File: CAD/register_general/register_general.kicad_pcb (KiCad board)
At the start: 4 copper layers, 76 x 28 mm, 29 parts, among them J1 Conn_01x16_Pin, J2 Conn_01x16_Pin, J3 load select, J4 output select, U1 74HC245, U2 74HC377

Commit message: add NetClasses, TestPads, remove jumper pins
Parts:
- removed J3: load select, Connector_PinHeader_2.54mm:PinHeader_1x03_P2.54mm_Vertical
- removed J4: output select, Connector_PinHeader_2.54mm:PinHeader_1x03_P2.54mm_Vertical
- added TP1: 5V, TestPoint:TestPoint_THTPad_D1.0mm_Drill0.5mm, F.Cu at (95.7, 68.2)
- added TP2: GND, TestPoint:TestPoint_THTPad_D1.0mm_Drill0.5mm, F.Cu at (91.7, 85.4)
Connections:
- J2 pad 1: reg2_out -> unconnected-(J2-Pin_1-Pad1)
- J2 pad 2: reg2_in -> unconnected-(J2-Pin_2-Pad2)
- J2 pad 3: reg1_out -> reg2_out
- J2 pad 4: reg1_in -> reg2_in
- R10 pad 1: Net-(J4-Pin_2) -> reg1_out
- R9 pad 1: Net-(J3-Pin_2) -> reg1_in
- U1 pad 19: Net-(J4-Pin_2) -> reg1_out
- U2 pad 1: Net-(J3-Pin_2) -> reg1_in
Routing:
- net Net-(J4-Pin_2): track 62.9 -> 0.00 mm, vias 3 -> 0
- net Net-(J3-Pin_2): track 46.0 -> 0.00 mm, vias 2 -> 0
- net reg1_in: track 71.0 -> 54.5 mm, vias 1 -> 2
- net reg1_out: track 65.1 -> 67.9 mm, vias 1 -> 2
- net +5V: track 148.9 -> 151.2 mm
- net reg2_in: track 69.5 -> 70.2 mm
- net GND: vias 106 -> 102
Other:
- copper layers 4 -> 2
- board text added: "5V"
- board text added: "GND"
- board text removed: "I"
- board text removed: "II"
- board text removed: "in"
- board text removed: "out"

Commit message: fix HC245 dir signal
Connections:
- U1 pad 1: GND -> +5V
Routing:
- net +5V: track 151.2 -> 154.8 mm
- net GND: vias 102 -> 104

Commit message: add text variables for revision, etc.
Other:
- board text added: "Rev ${REVISION} ${YEAR}/${MONTH}"
- board text removed: "Rev 1.0 2026/03"
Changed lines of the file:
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@@
 		)
 	)
+	(property "DAY" "03")
+	(property "MONTH" "03")
+	(property "REVISION" "1.0")
+	(property "YEAR" "2026")
 	(net 0 "")
 	(net 1 "GND")
@@
 		)
 	)
-	(gr_text "Rev 1.0\n2026/03"
+	(gr_text "Rev ${REVISION}\n${YEAR}/${MONTH}"
 		(at 152.65 80.335001 90)
 		(layer "B.SilkS" knockout)

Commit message: update silkscreen qr code, license, add images
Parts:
- added G***: Github QR Code, LOGO, B.Cu at (112.4, 86.6)
- added Ref**: Val**, 8-bit_computer:by-nc-sa.eu, B.Cu at (112.5, 69.6)
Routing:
- net GND: vias 104 -> 103

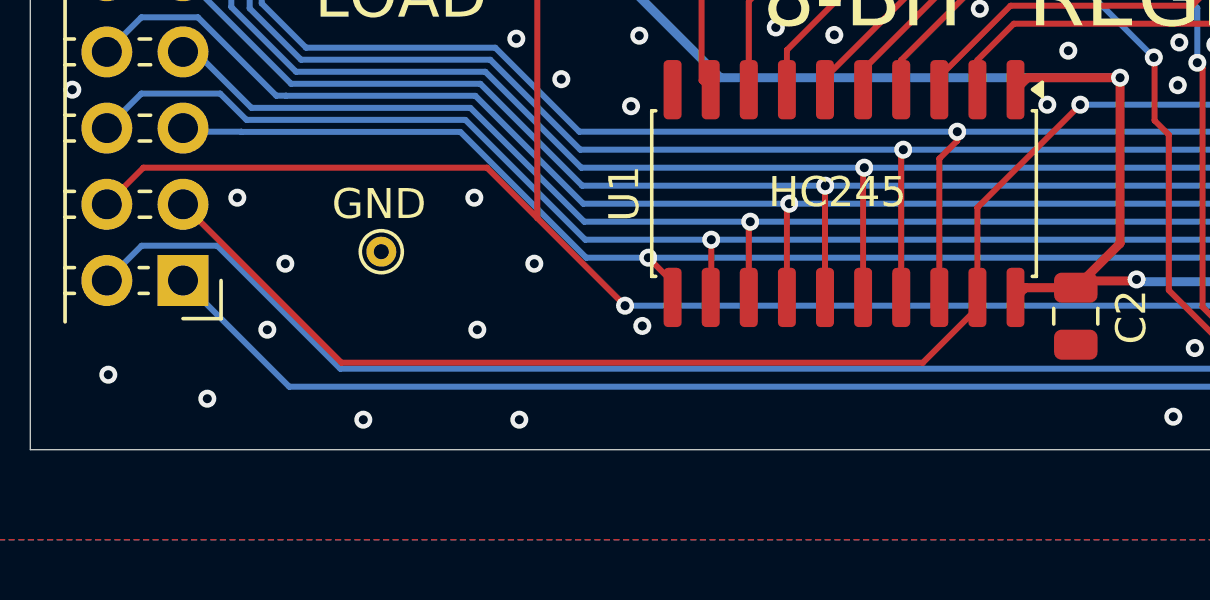
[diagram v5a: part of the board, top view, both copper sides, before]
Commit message: add pull-up resistor to general register
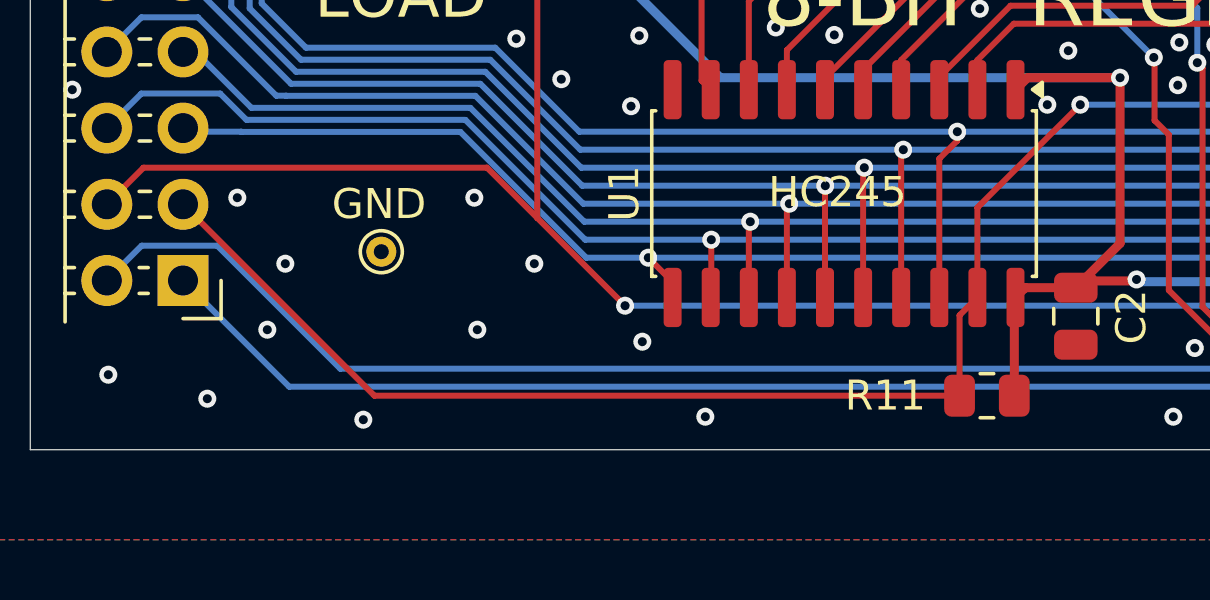
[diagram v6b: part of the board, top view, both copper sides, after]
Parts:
- added R11: 10k, Resistor_SMD:R_0805_2012Metric, F.Cu at (111.9, 90.2)
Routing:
- net +5V: track 154.8 -> 158.1 mm
- net reg1_out: track 67.9 -> 70.5 mm

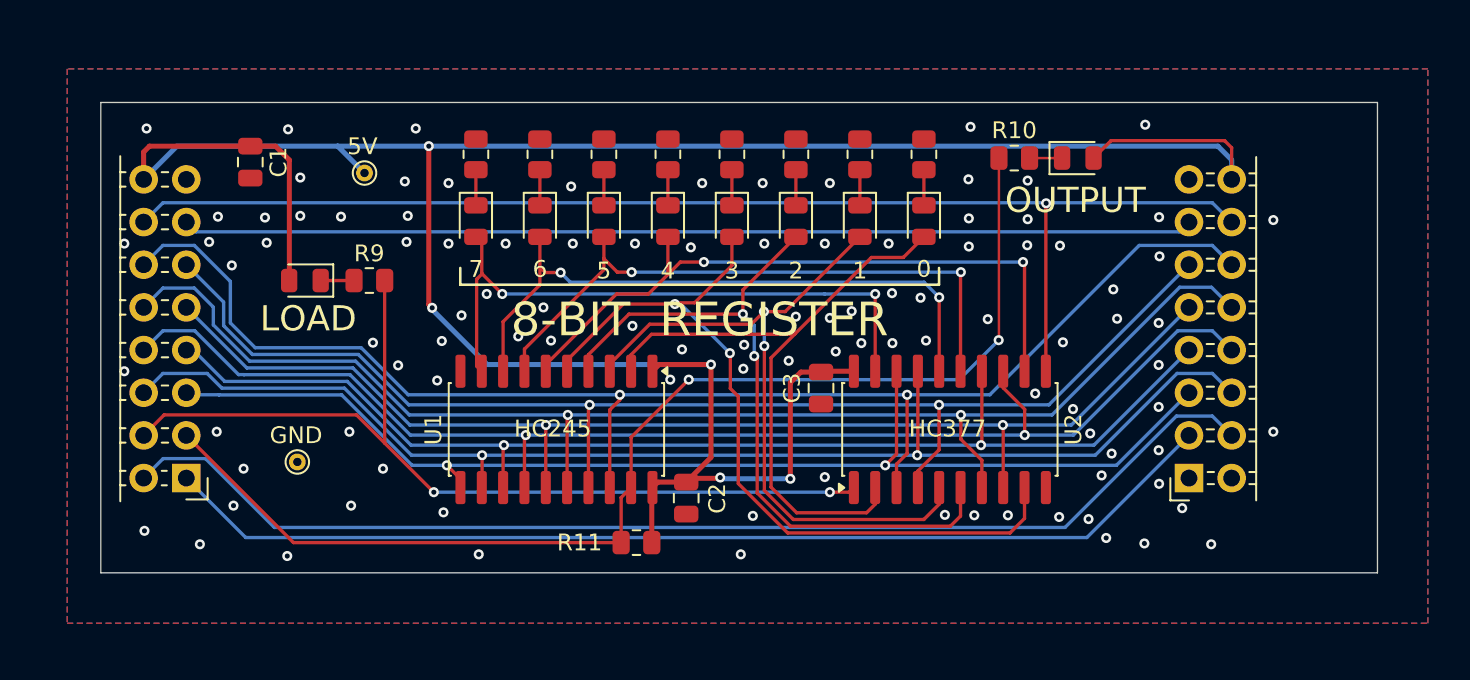
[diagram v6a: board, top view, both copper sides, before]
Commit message: update General Register, add mounting holes, testpoints, LCSC numbers
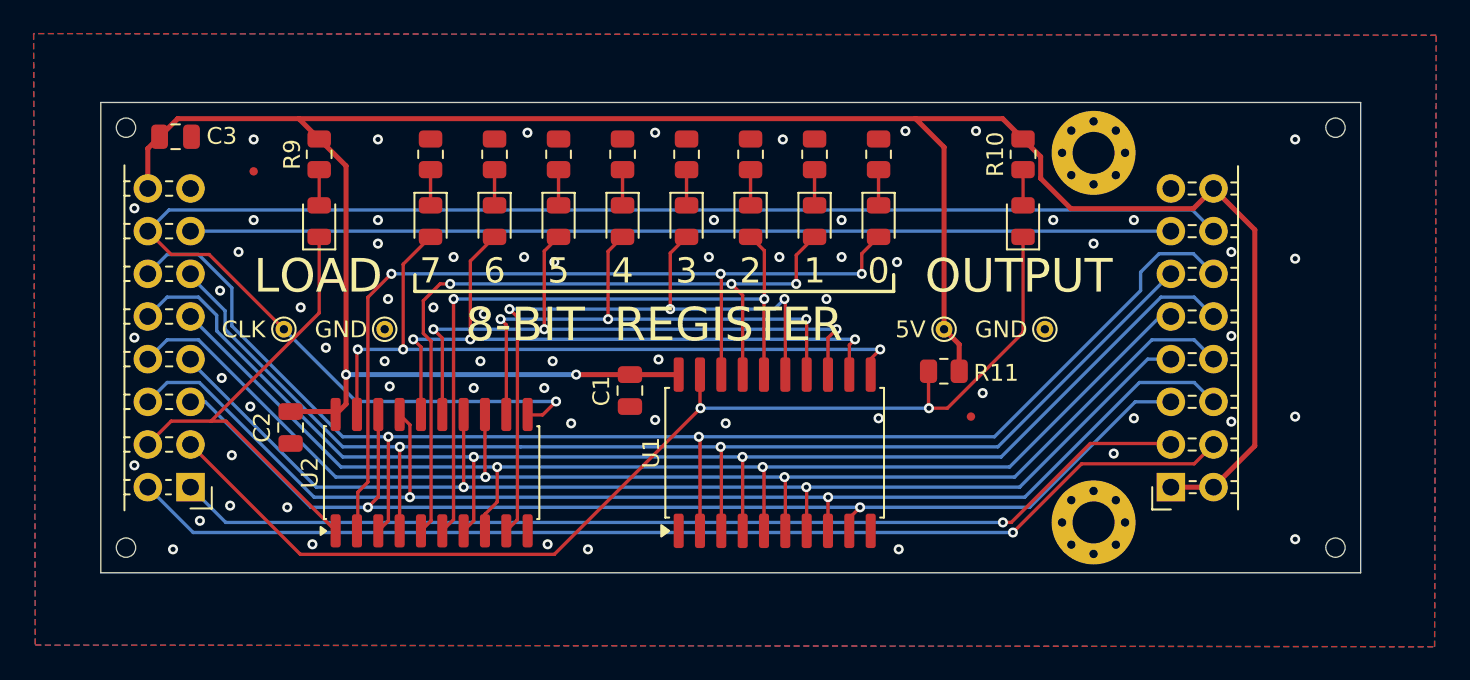
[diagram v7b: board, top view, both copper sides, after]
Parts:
- removed the G*** at (112.4, 86.6)
- added FID1: Fiducial, Fiducial:Fiducial_0.5mm_Mask1mm, F.Cu at (89.1, 68.1)
- added FID2: Fiducial, Fiducial:Fiducial_0.5mm_Mask1mm, F.Cu at (131.8, 82.7)
- added G***: LOGO, 8-bit_computer:qr-code-github, B.Cu at (111.4, 70.3)
- added H1: MountingHole_Pad, MountingHole:MountingHole_2.5mm_Pad_Via, F.Cu at (139.1, 89.0)
- added H2: MountingHole_Pad, MountingHole:MountingHole_2.5mm_Pad_Via, F.Cu at (139.1, 67.0)
- added H3: ToolingHole, MountingHole:ToolingHole_1.152mm, F.Cu at (81.5, 65.5)
- added H4: ToolingHole, MountingHole:ToolingHole_1.152mm, F.Cu at (81.5, 90.5)
- added H5: ToolingHole, MountingHole:ToolingHole_1.152mm, F.Cu at (153.5, 65.5)
- added H6: ToolingHole, MountingHole:ToolingHole_1.152mm, F.Cu at (153.5, 90.5)
- added TP3: TestPoint, TestPoint:TestPoint_THTPad_D1.0mm_Drill0.5mm, F.Cu at (90.9, 77.5)
- added TP4: TestPoint, TestPoint:TestPoint_THTPad_D1.0mm_Drill0.5mm, F.Cu at (96.9, 77.5)
- D10: value LED -> OUT
- D9: value LED -> IN
- TP1: value 5V -> TestPoint
- TP2: value GND -> TestPoint
- U1: footprint Package_SO:SO-20_5.3x12.6mm_P1.27mm -> Package_SO:SOIC-20W_7.5x12.8mm_P1.27mm
- U2: footprint Package_SO:SO-20_5.3x12.6mm_P1.27mm -> 8-bit_computer:SO-20_5.3x12.6mm_P1.27mm
- moved TP2 45.2 mm to (136.2, 77.5)
- moved TP1 35.7 mm to (130.2, 77.5)
- moved C2 31.7 mm to (91.3, 83.3)
- moved U2 31.0 mm to (99.7, 86.0)
- moved Ref** 23.0 mm to (132.0, 81.8)
- moved R11 21.0 mm to (130.2, 80.0)
- moved U1 13.1 mm to (120.1, 84.8), turned to 90 degrees
- moved R9 8.08 mm to (93.0, 67.1), turned to -90 degrees
- moved C1 7.22 mm to (111.5, 81.2)
- moved D10 4.97 mm to (134.9, 71.1), turned to 90 degrees
- moved C3 4.70 mm to (84.5, 66.0), turned to 0 degrees
- moved D9 3.64 mm to (93.0, 71.1), turned to 90 degrees
- moved D1 2.70 mm to (126.3, 71.1)
- moved D2 2.70 mm to (122.5, 71.1)
- moved D5 2.70 mm to (111.1, 71.1)
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- renumbered C2 to C1, C3 to C2, C1 to C3
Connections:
- net reg2_in renamed ~{reg2_in}
- net reg2_out renamed ~{reg2_out}
- net rst renamed ~{rst}
- D10 pad 1: Net-(D10-K) -> ~{reg1_out}
- D10 pad 2: +5V -> Net-(D10-A)
- D9 pad 1: Net-(D9-K) -> ~{reg1_in}
- D9 pad 2: +5V -> Net-(D9-A)
- J1 pad 3: reg1_out -> ~{reg1_out}
- J1 pad 4: reg1_in -> ~{reg1_in}
- J2 pad 1: unconnected-(J2-Pin_1-Pad1) -> +5V
- J2 pad 2: unconnected-(J2-Pin_2-Pad2) -> +5V
- R10 pad 1: reg1_out -> Net-(D10-A)
- R10 pad 2: Net-(D10-K) -> +5V
- R11 pad 1: reg1_out -> ~{reg1_out}
- R9 pad 1: reg1_in -> +5V
- R9 pad 2: Net-(D9-K) -> Net-(D9-A)
- U1 pad 1: +5V -> GND
- U1 pad 11: /dbus7 -> /q7
- U1 pad 12: /dbus6 -> /q6
- U1 pad 13: /dbus5 -> /q5
- U1 pad 14: /dbus4 -> /q4
- U1 pad 15: /dbus3 -> /q3
- U1 pad 16: /dbus2 -> /q2
- U1 pad 17: /dbus1 -> /q1
- U1 pad 18: /dbus0 -> /q0
- U1 pad 19: reg1_out -> ~{reg1_out}
- U1 pad 2: /q0 -> /dbus0
- U1 pad 3: /q1 -> /dbus1
- U1 pad 4: /q2 -> /dbus2
- U1 pad 5: /q3 -> /dbus3
- U1 pad 6: /q4 -> /dbus4
- U1 pad 7: /q5 -> /dbus5
- U1 pad 8: /q6 -> /dbus6
- U1 pad 9: /q7 -> /dbus7
- U2 pad 1: reg1_in -> ~{reg1_in}
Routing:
- net reg1_out: track 70.5 -> 0.00 mm, vias 2 -> 0
- net ~{reg1_out}: track 0.00 -> 67.7 mm, vias 0 -> 2
- net reg1_in: track 54.5 -> 0.00 mm, vias 2 -> 0
- net ~{reg1_in}: track 0.00 -> 28.1 mm
- net clk: track 75.8 -> 95.0 mm
- net /q0: track 39.0 -> 52.8 mm, vias 0 -> 3
- net +5V: track 158.1 -> 150.1 mm, vias 5 -> 2
- net /q7: track 36.4 -> 44.1 mm, vias 2 -> 3
- net /q3: track 46.8 -> 39.5 mm, vias 2 -> 3
- net /q4: track 39.7 -> 32.6 mm, vias 2 -> 3
- net /q1: track 41.2 -> 45.7 mm, vias 2 -> 3
- net ~{reg2_in}: track 70.2 -> 66.7 mm, vias 0 -> 1
- net ~{reg2_out}: track 63.7 -> 61.2 mm, vias 0 -> 1
- net Net-(D9-A): track 0.00 -> 2.12 mm
- net Net-(D10-A): track 0.00 -> 2.12 mm
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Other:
- board size 76 x 28 mm -> 75 x 28 mm
- board text added: "CLK"
- board text added: "S/N"
- board text added: "github.com/${GITHUB}"
- board text removed: "HC245"
- board text removed: "HC377"

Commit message: update general register layout
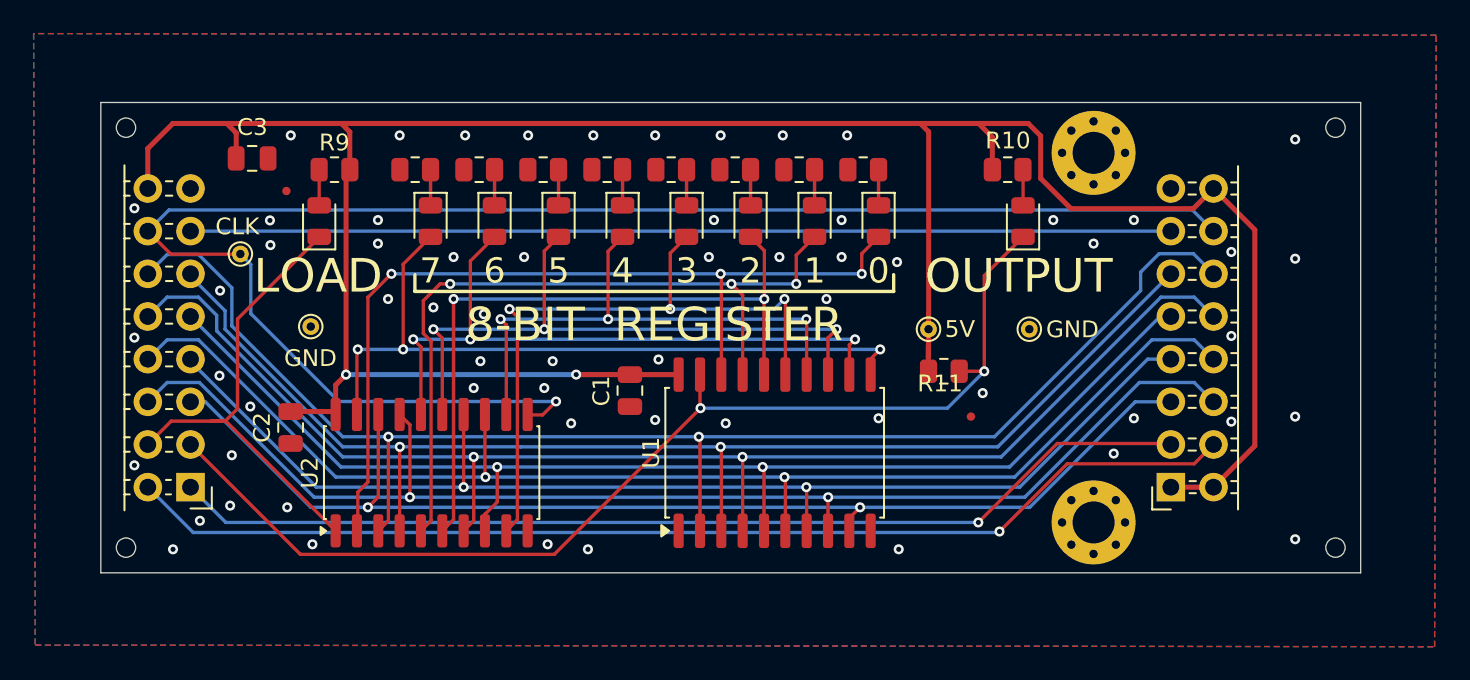
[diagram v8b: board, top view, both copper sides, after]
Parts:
- moved TP3 5.17 mm to (88.3, 73.0)
- moved C3 4.74 mm to (89.0, 67.3)
- moved TP4 4.40 mm to (92.5, 77.3)
- moved FID1 2.27 mm to (91.0, 69.3)
- moved R3 1.29 mm to (117.8, 68.0), turned to 180 degrees
- moved R4 1.29 mm to (114.0, 68.0), turned to 180 degrees
- moved R5 1.29 mm to (110.1, 68.0), turned to 180 degrees
- moved R1 1.29 mm to (125.4, 68.0), turned to 180 degrees
- moved R10 1.29 mm to (134.0, 68.0), turned to 180 degrees
- moved R2 1.29 mm to (121.6, 68.0), turned to 180 degrees
- moved R6 1.29 mm to (106.3, 68.0), turned to 180 degrees
- moved R7 1.29 mm to (102.5, 68.0), turned to 180 degrees
- moved R8 1.29 mm to (98.7, 68.0), turned to 180 degrees
- moved R9 1.29 mm to (93.9, 68.0), turned to 180 degrees
- moved TP1 0.93 mm to (129.3, 77.5)
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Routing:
- net +5V: track 150.1 -> 154.5 mm
- net clk: track 95.0 -> 96.6 mm
- net /dbus7: track 71.0 -> 70.2 mm
- net ~{reg1_out}: track 67.7 -> 66.9 mm
- net /dbus3: track 73.7 -> 73.1 mm
- net GND: vias 65 -> 62
